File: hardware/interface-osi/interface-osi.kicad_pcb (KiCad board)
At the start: 2 copper layers, 124.5 x 132.1 mm, 79 parts, among them J1 KBD port, J2 Key Matrix, J3 Expansion, J4 Sound, J5 ~RESET~, U1 74LS138, U10 74HC14, U11 4066, U2 74LS04, U3 74HC240, U4 74HC240, U5 74LS373, U6 74LS373, U7 74LS193, U8 74LS193, U9 74LS390

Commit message: More Interface-ASCII PCB cleanups
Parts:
- J5: value ~RESET~ -> ~{RESET}
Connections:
- net /R-~W renamed /R-~{W}
- net /special_keys/~RESET renamed /special_keys/~{RESET}
- net /~A0 renamed /~{A0}
- net /~A1 renamed /~{A1}
- net /~KBE renamed /~{KBE}
- net /~S1 renamed /~{S1}
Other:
- net class Default removed
- net class power1 removed
- net class signal removed
- board text added: "~{S1}"
- board text removed: "~S1"

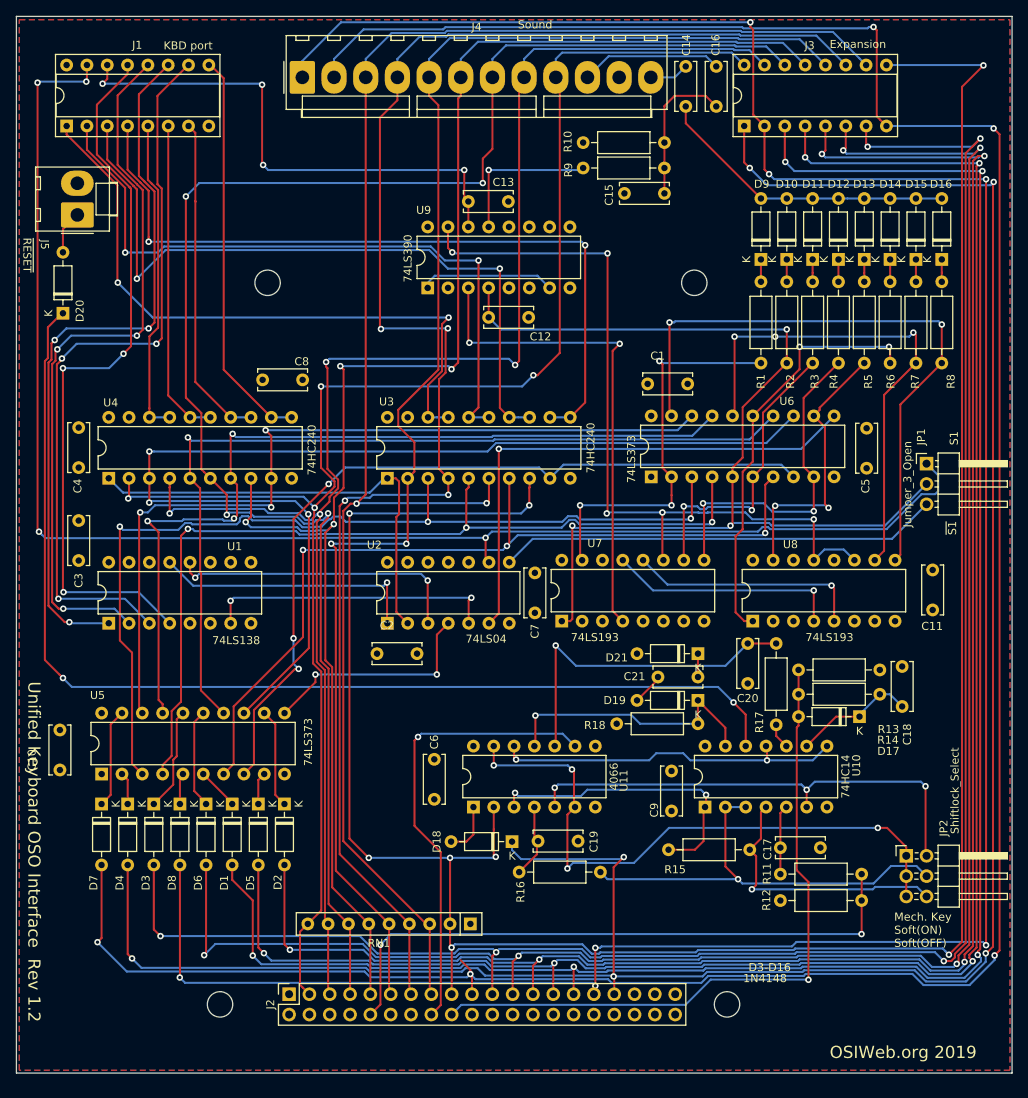
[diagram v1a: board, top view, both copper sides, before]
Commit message: ERC fixes
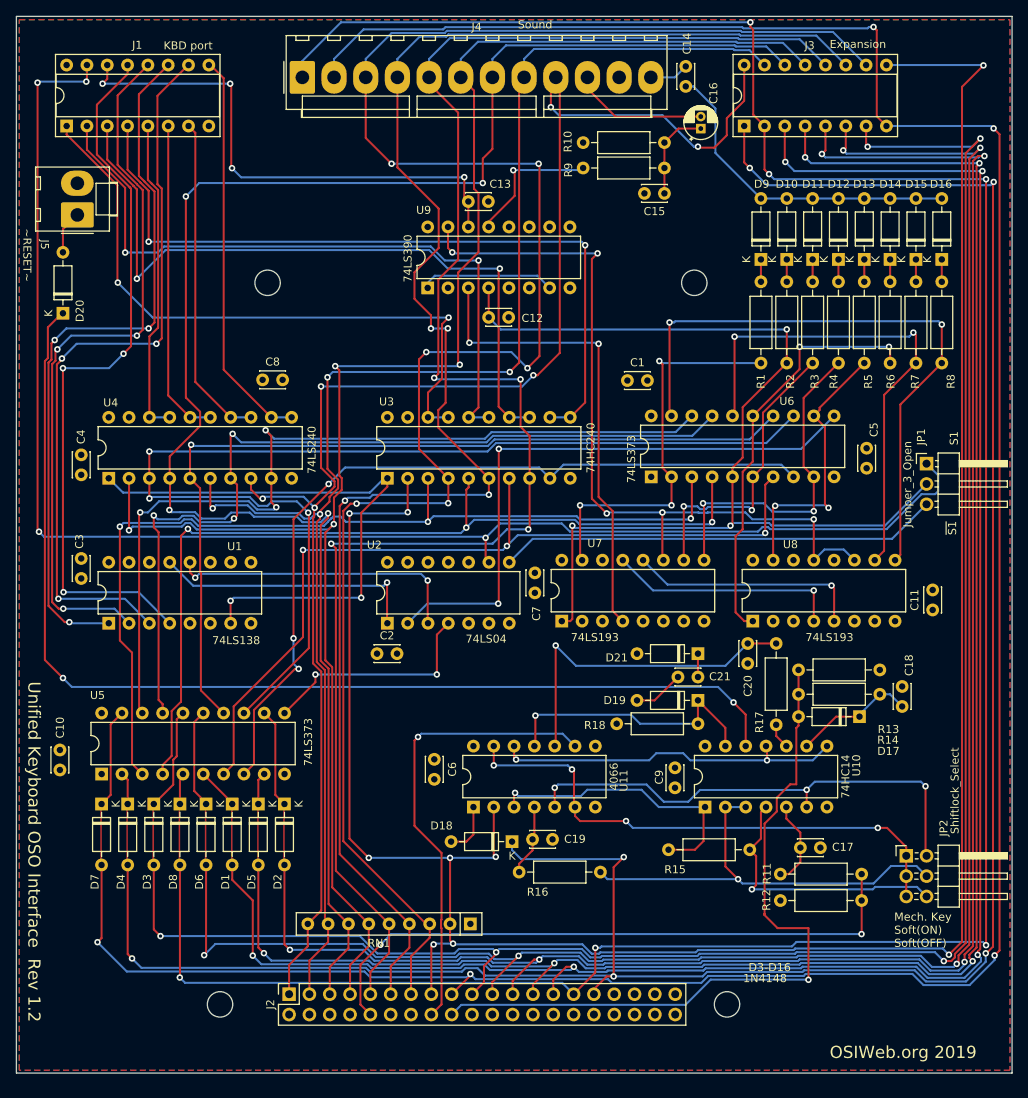
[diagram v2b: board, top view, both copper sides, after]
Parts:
- C1, C10, C11, C12, C13, C14, C17, C18, C19, C2, C20, C21, C3, C4, C5, C6, C7, C8, C9: footprint Capacitor_THT:C_Disc_D6.0mm_W2.5mm_P5.00mm -> Capacitor_THT:C_Disc_D3.0mm_W2.0mm_P2.50mm
- C15: value C -> 0.1uF; footprint Capacitor_THT:C_Disc_D6.0mm_W2.5mm_P5.00mm -> Capacitor_THT:C_Disc_D3.0mm_W2.0mm_P2.50mm
- C16: value C -> 33 uF; footprint Capacitor_THT:C_Disc_D6.0mm_W2.5mm_P5.00mm -> Capacitor_THT:CP_Radial_D4.0mm_P1.50mm
- D1, D2, D3, D4, D5, D6, D7, D8: footprint Diode_THT:D_DO-35_SOD27_P7.62mm_Horizontal -> unikbd:D_DO-35_SOD27_P7.62mm_Horizontal_bypassed
- J5: value ~{RESET} -> ~RESET~
- R10: value R_US -> 1k
- R9: value R_US -> 4.7k
- U4: value 74HC240 -> 74LS240
- moved C16 8.01 mm to (236.7, 64.8), turned to 90 degrees
- moved C3 4.75 mm to (159.2, 118.6)
- moved C4 3.42 mm to (159.2, 105.6)
- moved C19 3.20 mm to (218.1, 153.7)
- moved C1 2.57 mm to (227.5, 96.3)
- moved C9 0.59 mm to (233.5, 144.7)
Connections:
- C16 pad 1: /Sound/Noise2 -> Net-(C15-Pad1)
- C16 pad 2: Net-(C15-Pad1) -> /Sound/Noise2
- J2 pad 1: Net-(J2-Pad1) -> /Col7
- J2 pad 11: /Col3 -> /Col2
- J2 pad 13: /Col2 -> /Col1
- J2 pad 15: /Col1 -> /Col0
- J2 pad 17: /Col0 -> /Row7
- J2 pad 19: /Row7 -> /Row6
- J2 pad 2: Net-(J2-Pad2) -> unconnected-(J2-Pin_2-Pad2)
- J2 pad 21: /Row6 -> /Row5
- J2 pad 22: Net-(J2-Pad22) -> unconnected-(J2-Pin_22-Pad22)
- J2 pad 23: /Row5 -> /Row4
- J2 pad 24: Net-(J2-Pad24) -> unconnected-(J2-Pin_24-Pad24)
- J2 pad 25: /Row4 -> /Row3
- J2 pad 26: Net-(J2-Pad26) -> unconnected-(J2-Pin_26-Pad26)
- J2 pad 27: /Row3 -> /Row2
- J2 pad 28: Net-(J2-Pad28) -> unconnected-(J2-Pin_28-Pad28)
- J2 pad 29: /Row2 -> /Row1
- J2 pad 3: /Col7 -> /Col6
- J2 pad 30: Net-(J2-Pad30) -> unconnected-(J2-Pin_30-Pad30)
- J2 pad 31: /Row1 -> /Row0
- J2 pad 32: Net-(J2-Pad32) -> unconnected-(J2-Pin_32-Pad32)
- J2 pad 33: /Row0 -> unconnected-(J2-Pin_33-Pad33)
- J2 pad 34: Net-(J2-Pad34) -> unconnected-(J2-Pin_34-Pad34)
- J2 pad 35: Net-(J2-Pad35) -> unconnected-(J2-Pin_35-Pad35)
- J2 pad 36: Net-(J2-Pad36) -> unconnected-(J2-Pin_36-Pad36)
- J2 pad 37: Net-(J2-Pad37) -> unconnected-(J2-Pin_37-Pad37)
- J2 pad 38: Net-(J2-Pad38) -> unconnected-(J2-Pin_38-Pad38)
- J2 pad 39: Net-(J2-Pad39) -> unconnected-(J2-Pin_39-Pad39)
- J2 pad 4: Net-(J2-Pad4) -> unconnected-(J2-Pin_4-Pad4)
- J2 pad 40: Net-(J2-Pad40) -> unconnected-(J2-Pin_40-Pad40)
- J2 pad 5: /Col6 -> /Col5
- J2 pad 6: Net-(J2-Pad6) -> unconnected-(J2-Pin_6-Pad6)
- J2 pad 7: /Col5 -> /Col4
- J2 pad 8: Net-(J2-Pad8) -> unconnected-(J2-Pin_8-Pad8)
- J2 pad 9: /Col4 -> /Col3
- U1 pad 10: Net-(U1-Pad10) -> unconnected-(U1-O5-Pad10)
- U1 pad 11: Net-(U1-Pad11) -> unconnected-(U1-O4-Pad11)
- U1 pad 14: Net-(U1-Pad14) -> unconnected-(U1-O1-Pad14)
- U1 pad 15: Net-(U1-Pad15) -> unconnected-(U1-O0-Pad15)
- U1 pad 7: Net-(U1-Pad7) -> Net-(U1-O7)
- U1 pad 9: Net-(U1-Pad9) -> unconnected-(U1-O6-Pad9)
- U2 pad 10: (no net) -> unconnected-(U2-Pad10)
- U2 pad 11: (no net) -> unconnected-(U2-Pad11)
- U2 pad 12: (no net) -> unconnected-(U2-Pad12)
- U2 pad 13: (no net) -> unconnected-(U2-Pad13)
- U2 pad 14: (no net) -> +5V
- U2 pad 2: Net-(U2-Pad2) -> /Sound/SOUND_EN
- U2 pad 5: Net-(U1-Pad7) -> unconnected-(U2-Pad5)
- U2 pad 6: /Sound/SOUND_EN -> unconnected-(U2-Pad6)
- U2 pad 7: (no net) -> GND
- U3 pad 1: Net-(U2-Pad2) -> Net-(U1-O7)
- U3 pad 2: /Col3 -> /Col0
- U3 pad 4: /Col2 -> /Col1
- U3 pad 6: /Col1 -> /Col2
- U3 pad 8: /Col0 -> /Col3
- U4 pad 1: Net-(U2-Pad2) -> Net-(U1-O7)
- U4 pad 2: /Col7 -> /Col4
- U4 pad 4: /Col6 -> /Col5
- U4 pad 6: /Col5 -> /Col6
- U4 pad 8: /Col4 -> /Col7
- U7 pad 2: Net-(U7-Pad2) -> unconnected-(U7-QB-Pad2)
- U7 pad 3: Net-(U7-Pad3) -> unconnected-(U7-QA-Pad3)
- U7 pad 6: Net-(U7-Pad6) -> unconnected-(U7-QC-Pad6)
- U7 pad 7: Net-(U7-Pad7) -> unconnected-(U7-QD-Pad7)
- U8 pad 12: Net-(U8-Pad12) -> unconnected-(U8-~{CO}-Pad12)
- U8 pad 2: Net-(U8-Pad2) -> unconnected-(U8-QB-Pad2)
- U8 pad 3: Net-(U8-Pad3) -> unconnected-(U8-QA-Pad3)
- U8 pad 6: Net-(U8-Pad6) -> unconnected-(U8-QC-Pad6)
- U8 pad 7: Net-(U8-Pad7) -> unconnected-(U8-QD-Pad7)
- U9 pad 10: Net-(U9-Pad10) -> unconnected-(U9B-Q2-Pad10)
- U9 pad 11: Net-(U9-Pad11) -> unconnected-(U9B-Q1-Pad11)
- U9 pad 5: Net-(U9-Pad5) -> unconnected-(U9A-Q1-Pad5)
- U9 pad 6: Net-(U9-Pad6) -> unconnected-(U9A-Q2-Pad6)
- U9 pad 9: Net-(U9-Pad9) -> unconnected-(U9B-Q3-Pad9)
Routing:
- net Net-(U1-O7): track 0.00 -> 71.5 mm, vias 0 -> 2
- net Net-(U2-Pad2): track 56.4 -> 0.00 mm
- net Net-(U1-Pad7): track 36.4 -> 0.00 mm, vias 2 -> 0
- net /Col1: track 208.6 -> 238.3 mm, vias 2 -> 6
- net /Col3: track 185.2 -> 210.5 mm, vias 2 -> 4
- net /Col4: track 198.0 -> 217.1 mm
- net /Col0: track 298.2 -> 285.8 mm, vias 8 -> 9
- net Net-(JP2-Pin_1): track 77.0 -> 67.4 mm
- net /Sound/SOUND_EN: track 65.9 -> 75.3 mm, vias 1 -> 2
- net /Col6: track 200.0 -> 191.6 mm
- net /Col5: track 210.0 -> 218.1 mm
- net Net-(C15-Pad1): track 18.5 -> 11.6 mm
- net /special_keys/Break_1: track 85.9 -> 92.0 mm
- net /Col7: track 199.4 -> 193.4 mm, vias 4 -> 6
- net /Col2: track 202.7 -> 207.7 mm
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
